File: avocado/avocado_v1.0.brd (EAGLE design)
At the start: 79 x 79 mm, 99 parts, among them IC1 TM4C129XXXPDT, IC3 MAX31855, IC4 ISO3088, J1 THERMOCOUPLE, U1 LMT87DCKT

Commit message: design that was ordered in first PCB run
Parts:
- renumbered U$13 to C51, U$8 to C50
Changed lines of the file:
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@@
 <grid distance="0.1" unitdist="mm" unit="mm" style="lines" multiple="1" display="yes" altdistance="0.05" altunitdist="mm" altunit="mm"/>
 <layers>
-<layer number="1" name="Top" color="4" fill="1" visible="yes" active="yes"/>
+<layer number="1" name="Top" color="4" fill="1" visible="no" active="yes"/>
 <layer number="2" name="Route2" color="1" fill="3" visible="yes" active="yes"/>
 <layer number="3" name="Route3" color="4" fill="3" visible="no" active="no"/>
@@
 <layer number="13" name="Route13" color="4" fill="5" visible="no" active="no"/>
 <layer number="14" name="Route14" color="1" fill="6" visible="no" active="no"/>
-<layer number="15" name="Route15" color="4" fill="6" visible="yes" active="yes"/>
-<layer number="16" name="Bottom" color="1" fill="1" visible="yes" active="yes"/>
+<layer number="15" name="Route15" color="4" fill="6" visible="no" active="yes"/>
+<layer number="16" name="Bottom" color="1" fill="1" visible="no" active="yes"/>
 <layer number="17" name="Pads" color="2" fill="1" visible="yes" active="yes"/>
 <layer number="18" name="Vias" color="2" fill="1" visible="yes" active="yes"/>
@@
 <attribute name="VALUE" x="-32.059809375" y="-9.356040625" size="0.8243375" layer="27" rot="R270"/>
 </element>
-<element name="U$13" library="avocado" package="UPJXXXXXMHD6" value="UPJXXXXXMHD6" x="6.07" y="-25.19" smashed="yes" rot="R270">
+<element name="C51" library="avocado" package="UPJXXXXXMHD6" value="UPJXXXXXMHD6" x="6.07" y="-25.19" smashed="yes" rot="R270">
 <attribute name="NAME" x="5.89" y="-25.53" size="1.27" layer="25" font="vector"/>
 </element>
@@
 </element>
 <element name="U$4" library="avocado" package="NX3225GA" value="NX3225GA" x="8.8136" y="33.921" rot="MR0"/>
-<element name="U$8" library="avocado" package="UPJXXXXXMHD6" value="UPJXXXXXMHD6" x="20.47" y="-13.04" smashed="yes" rot="R270">
+<element name="C50" library="avocado" package="UPJXXXXXMHD6" value="UPJXXXXXMHD6" x="20.47" y="-13.04" smashed="yes" rot="R270">
 <attribute name="NAME" x="19.34" y="-13.53" size="1.27" layer="25" font="vector"/>
 </element>
@@
 <contactref element="C6" pad="1"/>
 <contactref element="C7" pad="1"/>
-<contactref element="U$8" pad="+"/>
-<contactref element="U$13" pad="+"/>
+<contactref element="C50" pad="+"/>
+<contactref element="C51" pad="+"/>
 <contactref element="J2" pad="2"/>
 <contactref element="J2" pad="1"/>
@@
 <vertex x="42.9" y="-9.8"/>
 </polygon>
-<via x="-21.5" y="-7.8" extent="1-2" drill="0.35"/>
-<via x="-20.4" y="-7.8" extent="1-2" drill="0.35"/>
-<via x="-19.3" y="-7.8" extent="1-2" drill="0.35"/>
-<via x="-18.2" y="-7.8" extent="1-2" drill="0.35"/>
-<via x="-17.1" y="-7.8" extent="1-2" drill="0.35"/>
-<via x="-16" y="-7.8" extent="1-2" drill="0.35"/>
-<via x="-14.9" y="-11.3" extent="1-2" drill="0.35"/>
-<via x="-21.5" y="-9" extent="1-2" drill="0.35"/>
-<via x="-20.4" y="-9" extent="1-2" drill="0.35"/>
-<via x="-19.3" y="-9" extent="1-2" drill="0.35"/>
-<via x="-18.2" y="-9" extent="1-2" drill="0.35"/>
-<via x="-17.1" y="-9" extent="1-2" drill="0.35"/>
-<via x="-16" y="-9" extent="1-2" drill="0.35"/>
-<via x="-21.5" y="-10.1" extent="1-2" drill="0.35"/>
-<via x="-20.4" y="-10.1" extent="1-2" drill="0.35"/>
-<via x="-19.3" y="-10.1" extent="1-2" drill="0.35"/>
-<via x="-18.2" y="-10.1" extent="1-2" drill="0.35"/>
-<via x="-17.1" y="-10.1" extent="1-2" drill="0.35"/>
-<via x="-16" y="-10.1" extent="1-2" drill="0.35"/>
-<via x="-21.5" y="-11.3" extent="1-2" drill="0.35"/>
-<via x="-20.4" y="-11.3" extent="1-2" drill="0.35"/>
-<via x="-19.3" y="-11.3" extent="1-2" drill="0.35"/>
-<via x="-18.2" y="-11.3" extent="1-2" drill="0.35"/>
-<via x="-17.1" y="-11.3" extent="1-2" drill="0.35"/>
-<via x="-16" y="-11.3" extent="1-2" drill="0.35"/>
-<via x="-18.2" y="-12.4" extent="1-2" drill="0.35"/>
-<via x="-17.1" y="-12.4" extent="1-2" drill="0.35"/>
-<via x="-16" y="-12.4" extent="1-2" drill="0.35"/>
-<via x="-14.9" y="-12.4" extent="1-2" drill="0.35"/>
-<via x="-13.8" y="-12.4" extent="1-2" drill="0.35"/>
-<via x="-12.7" y="-12.4" extent="1-2" drill="0.35"/>
-<via x="-18.2" y="-13.6" extent="1-2" drill="0.35"/>
-<via x="-17.1" y="-13.6" extent="1-2" drill="0.35"/>
-<via x="-16" y="-13.6" extent="1-2" drill="0.35"/>
-<via x="-14.9" y="-13.6" extent="1-2" drill="0.35"/>
-<via x="-13.8" y="-13.6" extent="1-2" drill="0.35"/>
-<via x="-12.7" y="-13.6" extent="1-2" drill="0.35"/>
-<via x="-17.1" y="-14.7" extent="1-2" drill="0.35"/>
-<via x="-16" y="-14.7" extent="1-2" drill="0.35"/>
-<via x="-14.9" y="-14.7" extent="1-2" drill="0.35"/>
-<via x="-13.8" y="-14.7" extent="1-2" drill="0.35"/>
-<via x="-12.7" y="-14.7" extent="1-2" drill="0.35"/>
-<via x="-11.6" y="-14.7" extent="1-2" drill="0.35"/>
-<via x="-17.1" y="-15.9" extent="1-2" drill="0.35"/>
-<via x="-16" y="-15.9" extent="1-2" drill="0.35"/>
-<via x="-14.9" y="-15.9" extent="1-2" drill="0.35"/>
-<via x="-13.8" y="-15.9" extent="1-2" drill="0.35"/>
-<via x="-12.7" y="-15.9" extent="1-2" drill="0.35"/>
-<via x="-11.6" y="-15.9" extent="1-2" drill="0.35"/>
+<via x="-21.5" y="-7.8" extent="1-16" drill="0.35"/>
+<via x="-20.4" y="-7.8" extent="1-16" drill="0.35"/>
+<via x="-19.3" y="-7.8" extent="1-16" drill="0.35"/>
+<via x="-18.2" y="-7.8" extent="1-16" drill="0.35"/>
+<via x="-17.1" y="-7.8" extent="1-16" drill="0.35"/>
+<via x="-16" y="-7.8" extent="1-16" drill="0.35"/>
+<via x="-14.9" y="-11.3" extent="1-16" drill="0.35"/>
+<via x="-21.5" y="-9" extent="1-16" drill="0.35"/>
+<via x="-20.4" y="-9" extent="1-16" drill="0.35"/>
+<via x="-19.3" y="-9" extent="1-16" drill="0.35"/>
+<via x="-18.2" y="-9" extent="1-16" drill="0.35"/>
+<via x="-17.1" y="-9" extent="1-16" drill="0.35"/>
+<via x="-16" y="-9" extent="1-16" drill="0.35"/>
+<via x="-21.5" y="-10.1" extent="1-16" drill="0.35"/>
+<via x="-20.4" y="-10.1" extent="1-16" drill="0.35"/>
+<via x="-19.3" y="-10.1" extent="1-16" drill="0.35"/>
+<via x="-18.2" y="-10.1" extent="1-16" drill="0.35"/>
+<via x="-17.1" y="-10.1" extent="1-16" drill="0.35"/>
+<via x="-16" y="-10.1" extent="1-16" drill="0.35"/>
+<via x="-21.5" y="-11.3" extent="1-16" drill="0.35"/>
+<via x="-20.4" y="-11.3" extent="1-16" drill="0.35"/>
+<via x="-19.3" y="-11.3" extent="1-16" drill="0.35"/>
+<via x="-18.2" y="-11.3" extent="1-16" drill="0.35"/>
+<via x="-17.1" y="-11.3" extent="1-16" drill="0.35"/>
+<via x="-16" y="-11.3" extent="1-16" drill="0.35"/>
+<via x="-18.2" y="-12.4" extent="1-16" drill="0.35"/>
+<via x="-17.1" y="-12.4" extent="1-16" drill="0.35"/>
+<via x="-16" y="-12.4" extent="1-16" drill="0.35"/>
+<via x="-14.9" y="-12.4" extent="1-16" drill="0.35"/>
+<via x="-13.8" y="-12.4" extent="1-16" drill="0.35"/>
+<via x="-12.7" y="-12.4" extent="1-16" drill="0.35"/>
+<via x="-18.2" y="-13.6" extent="1-16" drill="0.35"/>
+<via x="-17.1" y="-13.6" extent="1-16" drill="0.35"/>
+<via x="-16" y="-13.6" extent="1-16" drill="0.35"/>
+<via x="-14.9" y="-13.6" extent="1-16" drill="0.35"/>
+<via x="-13.8" y="-13.6" extent="1-16" drill="0.35"/>
+<via x="-12.7" y="-13.6" extent="1-16" drill="0.35"/>
+<via x="-17.1" y="-14.7" extent="1-16" drill="0.35"/>
+<via x="-16" y="-14.7" extent="1-16" drill="0.35"/>
+<via x="-14.9" y="-14.7" extent="1-16" drill="0.35"/>
+<via x="-13.8" y="-14.7" extent="1-16" drill="0.35"/>
+<via x="-12.7" y="-14.7" extent="1-16" drill="0.35"/>
+<via x="-11.6" y="-14.7" extent="1-16" drill="0.35"/>
+<via x="-17.1" y="-15.9" extent="1-16" drill="0.35"/>
+<via x="-16" y="-15.9" extent="1-16" drill="0.35"/>
+<via x="-14.9" y="-15.9" extent="1-16" drill="0.35"/>
+<via x="-13.8" y="-15.9" extent="1-16" drill="0.35"/>
+<via x="-12.7" y="-15.9" extent="1-16" drill="0.35"/>
+<via x="-11.6" y="-15.9" extent="1-16" drill="0.35"/>
 <via x="-15.4" y="-23.9" extent="1-2" drill="0.35"/>
 <via x="-15.4" y="-22.8" extent="1-2" drill="0.35"/>
@@
 <contactref element="C38" pad="2"/>
 <contactref element="C40" pad="2"/>
-<contactref element="U$8" pad="-"/>
-<contactref element="U$13" pad="-"/>
+<contactref element="C50" pad="-"/>
+<contactref element="C51" pad="-"/>
 <contactref element="U$2" pad="1"/>
 <contactref element="J2" pad="4"/>

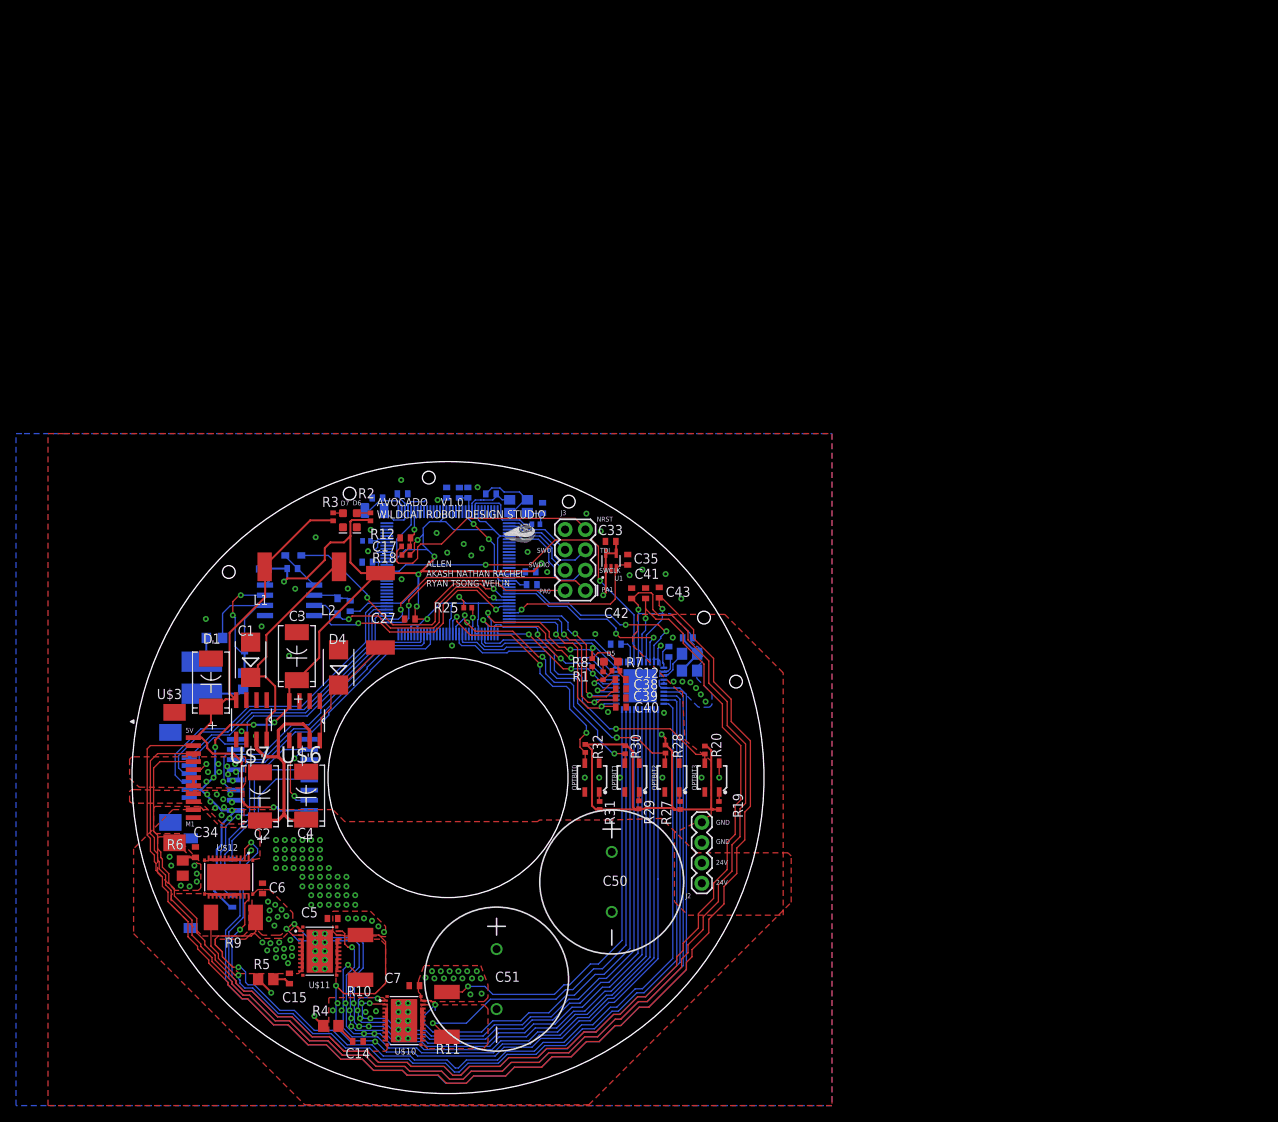
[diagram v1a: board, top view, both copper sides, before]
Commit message: removed blind vias and generated new Gerber files
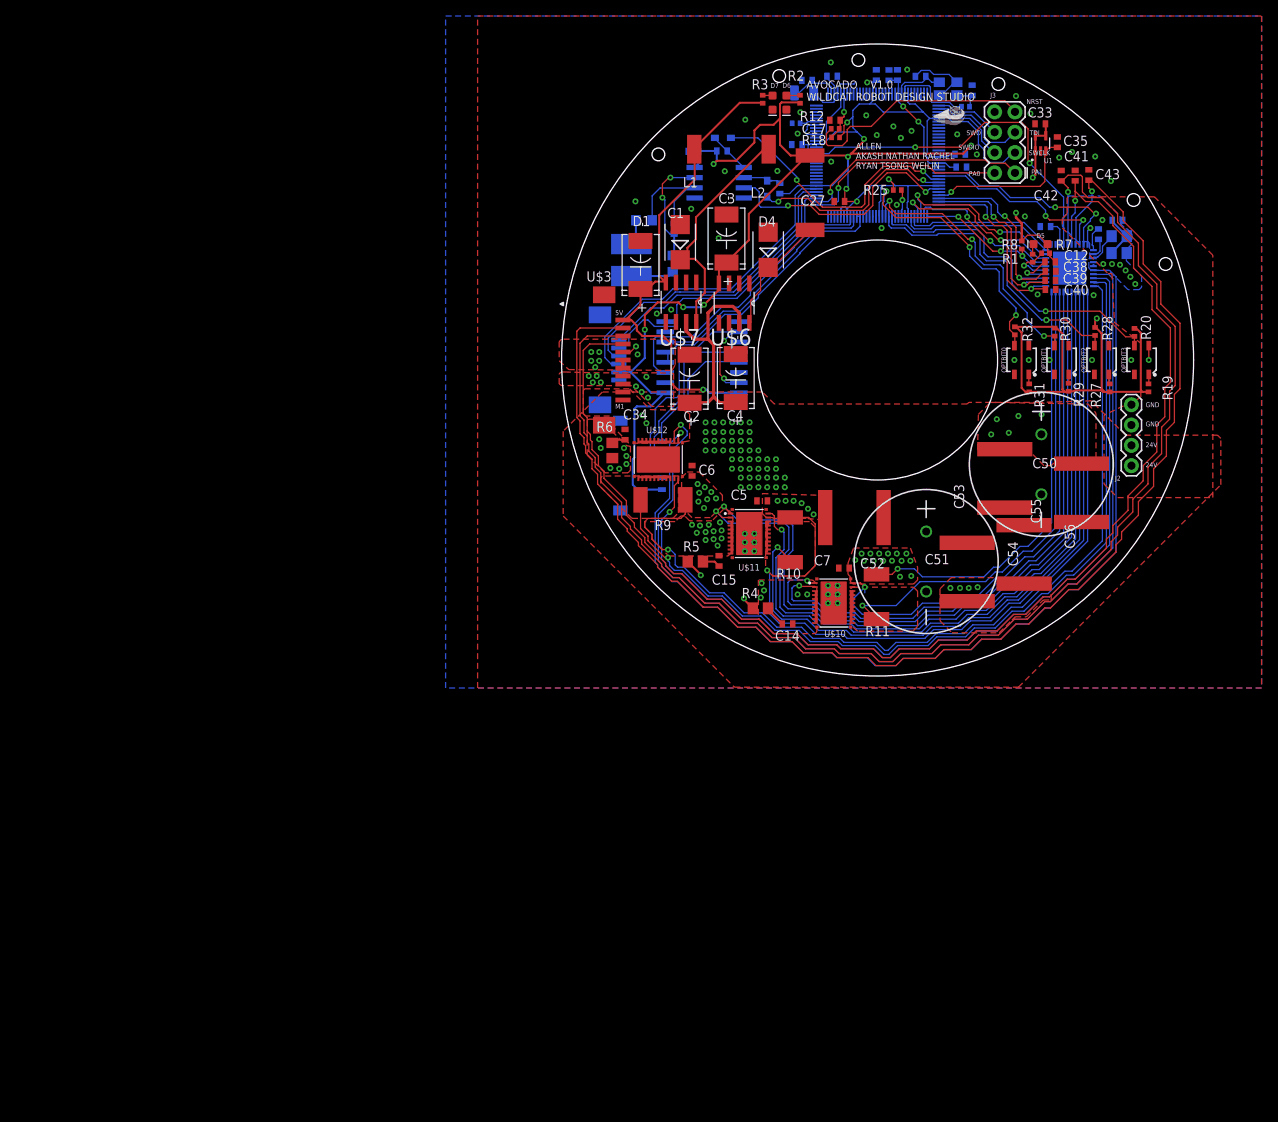
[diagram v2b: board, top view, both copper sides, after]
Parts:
- added C52, C53, C54, C55, C56: C7563, avocado:3025
- moved C1 74.9 mm to (24.1, 64.1)
- moved C10 74.9 mm to (83.9, 67.7)
- moved C11 74.9 mm to (81.3, 67.9)
- moved C12 74.9 mm to (75.3, 64.5)
- moved C13 74.9 mm to (74.7, 68.9)
- moved C14 74.9 mm to (42.4, 19.2)
- moved C15 74.9 mm to (33.9, 27.1)
- moved C17 74.9 mm to (48.4, 82.2)
- moved C18 74.9 mm to (43.6, 79.1)
- moved C19 74.9 mm to (30.7, 78.3)
- moved C2 74.9 mm to (30.2, 49.9)
- moved C20 74.9 mm to (53.5, 87.8)
- moved C21 74.9 mm to (55.1, 87.8)
- moved C22 74.9 mm to (59.1, 87.7)
- moved C23 74.9 mm to (65.5, 85.9)
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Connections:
- net 24VDC: now also C52.P$1, C53.P$1, C54.P$1, C55.P$1, C56.P$1
- net GND: now also C52.P$2, C53.P$2, C54.P$2, C55.P$2, C56.P$2
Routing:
- net 3V3DC: track 326.6 -> 330.6 mm
- net PE0: track 32.2 -> 34.8 mm
- net GND: track 279.6 -> 277.5 mm, vias 79 -> 88
- net 24VDC: vias 76 -> 68
- net M3: vias 30 -> 11

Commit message: new gerber files and updated peripheral/main board
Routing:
- net GND: vias 88 -> 85
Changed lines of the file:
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@@
 <setting verticaltext="up"/>
 </settings>
-<grid distance="3.93700787" unitdist="mil" unit="mil" style="lines" multiple="1" display="yes" altdistance="0.05" altunitdist="mm" altunit="mm"/>
+<grid distance="0.0999999999" unitdist="mm" unit="mm" style="lines" multiple="1" display="yes" altdistance="0.05" altunitdist="mm" altunit="mm"/>
 <layers>
 <layer number="1" name="Top" color="4" fill="1" visible="yes" active="yes"/>
-<layer number="2" name="Route2" color="1" fill="3" visible="yes" active="yes"/>
+<layer number="2" name="Route2" color="1" fill="3" visible="no" active="yes"/>
 <layer number="3" name="Route3" color="4" fill="3" visible="no" active="no"/>
 <layer number="4" name="Route4" color="1" fill="4" visible="no" active="no"/>
@@
 <layer number="13" name="Route13" color="4" fill="5" visible="no" active="no"/>
 <layer number="14" name="Route14" color="1" fill="6" visible="no" active="no"/>
-<layer number="15" name="Route15" color="4" fill="6" visible="yes" active="yes"/>
-<layer number="16" name="Bottom" color="1" fill="1" visible="yes" active="yes"/>
+<layer number="15" name="Route15" color="4" fill="6" visible="no" active="yes"/>
+<layer number="16" name="Bottom" color="1" fill="1" visible="no" active="yes"/>
 <layer number="17" name="Pads" color="2" fill="1" visible="yes" active="yes"/>
 <layer number="18" name="Vias" color="2" fill="1" visible="yes" active="yes"/>
@@
 <layer number="25" name="tNames" color="7" fill="1" visible="yes" active="yes"/>
 <layer number="26" name="bNames" color="7" fill="1" visible="yes" active="yes"/>
-<layer number="27" name="tValues" color="7" fill="1" visible="no" active="yes"/>
-<layer number="28" name="bValues" color="7" fill="1" visible="no" active="yes"/>
+<layer number="27" name="tValues" color="7" fill="1" visible="yes" active="yes"/>
+<layer number="28" name="bValues" color="7" fill="1" visible="yes" active="yes"/>
 <layer number="29" name="tStop" color="7" fill="3" visible="no" active="yes"/>
 <layer number="30" name="bStop" color="7" fill="6" visible="no" active="yes"/>
@@
 </polygon>
 <via x="18.9" y="42.3" extent="1-16" drill="0.35"/>
-<via x="19.1" y="41.2" extent="1-16" drill="0.35"/>
-<via x="20.3" y="38.7" extent="1-16" drill="0.35"/>
-<via x="21.4" y="38.6" extent="1-16" drill="0.35"/>
 <via x="22.3" y="39.2" extent="1-16" drill="0.35"/>
 <via x="22.3" y="40.2" extent="1-16" drill="0.35"/>

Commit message: added v2.0 of the avocado main pcb
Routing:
- net H1: track 172.0 -> 171.2 mm
- net 24VDC: vias 68 -> 31
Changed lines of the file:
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@@
 <setting verticaltext="up"/>
 </settings>
-<grid distance="0.0999999999" unitdist="mm" unit="mm" style="lines" multiple="1" display="yes" altdistance="0.05" altunitdist="mm" altunit="mm"/>
+<grid distance="3.93700787" unitdist="mil" unit="mil" style="lines" multiple="1" display="yes" altdistance="0.05" altunitdist="mm" altunit="mm"/>
 <layers>
 <layer number="1" name="Top" color="4" fill="1" visible="yes" active="yes"/>
-<layer number="2" name="Route2" color="1" fill="3" visible="no" active="yes"/>
+<layer number="2" name="Route2" color="1" fill="3" visible="yes" active="yes"/>
 <layer number="3" name="Route3" color="4" fill="3" visible="no" active="no"/>
 <layer number="4" name="Route4" color="1" fill="4" visible="no" active="no"/>
@@
 <layer number="13" name="Route13" color="4" fill="5" visible="no" active="no"/>
 <layer number="14" name="Route14" color="1" fill="6" visible="no" active="no"/>
-<layer number="15" name="Route15" color="4" fill="6" visible="no" active="yes"/>
-<layer number="16" name="Bottom" color="1" fill="1" visible="no" active="yes"/>
+<layer number="15" name="Route15" color="4" fill="6" visible="yes" active="yes"/>
+<layer number="16" name="Bottom" color="1" fill="1" visible="yes" active="yes"/>
 <layer number="17" name="Pads" color="2" fill="1" visible="yes" active="yes"/>
 <layer number="18" name="Vias" color="2" fill="1" visible="yes" active="yes"/>
@@
 <vertex x="96.6" y="42.4"/>
 </polygon>
-<via x="32.2" y="44.4" extent="1-16" drill="0.35"/>
 <via x="33.3" y="44.4" extent="1-16" drill="0.35"/>
-<via x="34.4" y="44.4" extent="1-16" drill="0.35"/>
 <via x="35.5" y="44.4" extent="1-16" drill="0.35"/>
-<via x="36.6" y="44.4" extent="1-16" drill="0.35"/>
 <via x="37.7" y="44.4" extent="1-16" drill="0.35"/>
-<via x="38.8" y="40.9" extent="1-16" drill="0.35"/>
-<via x="32.2" y="43.2" extent="1-16" drill="0.35"/>
-<via x="33.3" y="43.2" extent="1-16" drill="0.35"/>
-<via x="34.4" y="43.2" extent="1-16" drill="0.35"/>
-<via x="35.5" y="43.2" extent="1-16" drill="0.35"/>
-<via x="36.6" y="43.2" extent="1-16" drill="0.35"/>
-<via x="37.7" y="43.2" extent="1-16" drill="0.35"/>
-<via x="32.2" y="42.1" extent="1-16" drill="0.35"/>
 <via x="33.3" y="42.1" extent="1-16" drill="0.35"/>
-<via x="34.4" y="42.1" extent="1-16" drill="0.35"/>
 <via x="35.5" y="42.1" extent="1-16" drill="0.35"/>
-<via x="36.6" y="42.1" extent="1-16" drill="0.35"/>
 <via x="37.7" y="42.1" extent="1-16" drill="0.35"/>
-<via x="32.2" y="40.9" extent="1-16" drill="0.35"/>
-<via x="33.3" y="40.9" extent="1-16" drill="0.35"/>
-<via x="34.4" y="40.9" extent="1-16" drill="0.35"/>
-<via x="35.5" y="40.9" extent="1-16" drill="0.35"/>
-<via x="36.6" y="40.9" extent="1-16" drill="0.35"/>
-<via x="37.7" y="40.9" extent="1-16" drill="0.35"/>
 <via x="35.5" y="39.8" extent="1-16" drill="0.35"/>
-<via x="36.6" y="39.8" extent="1-16" drill="0.35"/>
 <via x="37.7" y="39.8" extent="1-16" drill="0.35"/>
-<via x="38.8" y="39.8" extent="1-16" drill="0.35"/>
 <via x="39.9" y="39.8" extent="1-16" drill="0.35"/>
-<via x="41" y="39.8" extent="1-16" drill="0.35"/>
-<via x="35.5" y="38.6" extent="1-16" drill="0.35"/>
-<via x="36.6" y="38.6" extent="1-16" drill="0.35"/>
-<via x="37.7" y="38.6" extent="1-16" drill="0.35"/>
-<via x="38.8" y="38.6" extent="1-16" drill="0.35"/>
-<via x="39.9" y="38.6" extent="1-16" drill="0.35"/>
-<via x="41" y="38.6" extent="1-16" drill="0.35"/>
-<via x="36.6" y="37.5" extent="1-16" drill="0.35"/>
 <via x="37.7" y="37.5" extent="1-16" drill="0.35"/>
-<via x="38.8" y="37.5" extent="1-16" drill="0.35"/>
 <via x="39.9" y="37.5" extent="1-16" drill="0.35"/>
-<via x="41" y="37.5" extent="1-16" drill="0.35"/>
 <via x="42.1" y="37.5" extent="1-16" drill="0.35"/>
-<via x="36.6" y="36.3" extent="1-16" drill="0.35"/>
-<via x="37.7" y="36.3" extent="1-16" drill="0.35"/>
-<via x="38.8" y="36.3" extent="1-16" drill="0.35"/>
-<via x="39.9" y="36.3" extent="1-16" drill="0.35"/>
-<via x="41" y="36.3" extent="1-16" drill="0.35"/>
-<via x="42.1" y="36.3" extent="1-16" drill="0.35"/>
 <via x="38.3" y="28.3" extent="1-16" drill="0.35"/>
 <via x="38.3" y="29.4" extent="1-16" drill="0.35"/>
@@
 <wire x1="88.6" y1="58.7" x2="88.6" y2="61.7" width="0.1524" layer="1"/>
 <wire x1="86.3" y1="64" x2="86.3" y2="66.8" width="0.1524" layer="1"/>
-<wire x1="21.87" y1="55.2" x2="17.4" y2="55.2" width="0.1524" layer="1"/>
 <wire x1="77.5" y1="73.3" x2="77.5" y2="73.2" width="0.1524" layer="16"/>
 <via x="77.5" y="73.2" extent="1-16" drill="0.35"/>
@@
 <wire x1="16.5" y1="54.3" x2="17.4" y2="55.2" width="0.1524" layer="1"/>
 <wire x1="16.5" y1="45.2" x2="16.5" y2="54.3" width="0.1524" layer="1"/>
+<wire x1="17.4" y1="55.2" x2="21" y2="55.2" width="0.1524" layer="1"/>
+<wire x1="21" y1="55.2" x2="21.87" y2="55.2" width="0" layer="19" extent="1-1"/>
 </signal>
 <signal name="H2">
